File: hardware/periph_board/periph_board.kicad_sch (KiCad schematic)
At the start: 32 parts, among them IC100 CD74HC4067SM96, IC101 LM2937ET-3.3_NOPB, IC102 MCP3221AxT-E_OT, J100 2x8 Socket Pins, J101 2x8 Plug Pins

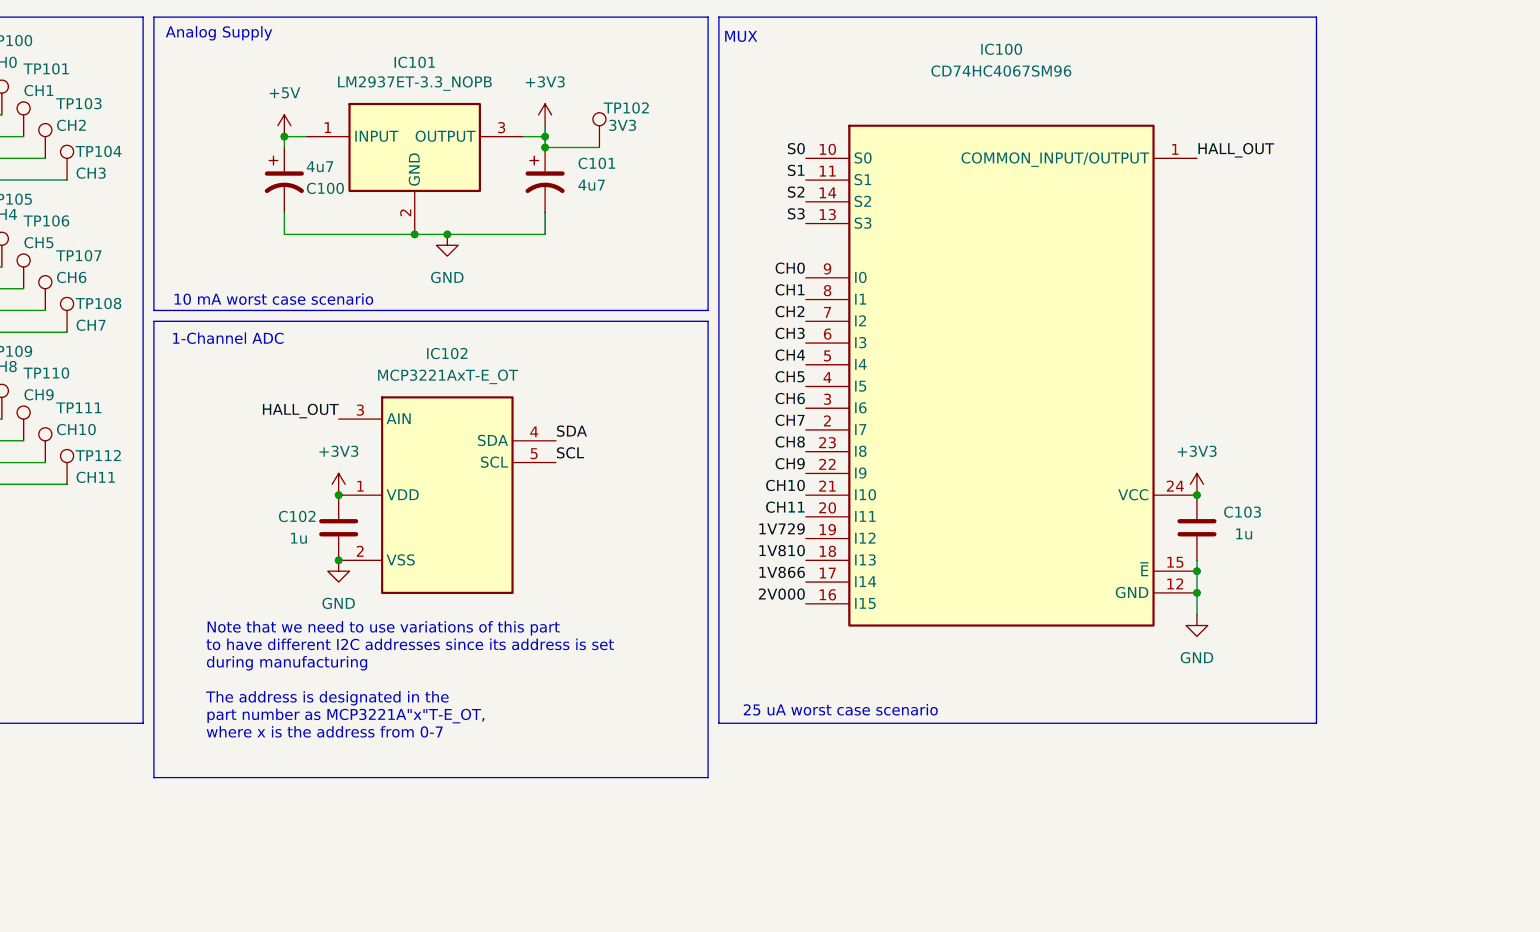
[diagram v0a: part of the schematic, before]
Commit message: added lakshay suggestions to peripheral board. removed bypass jumper from main board audio amp. added led strip interface. added too many things to remember i forgor
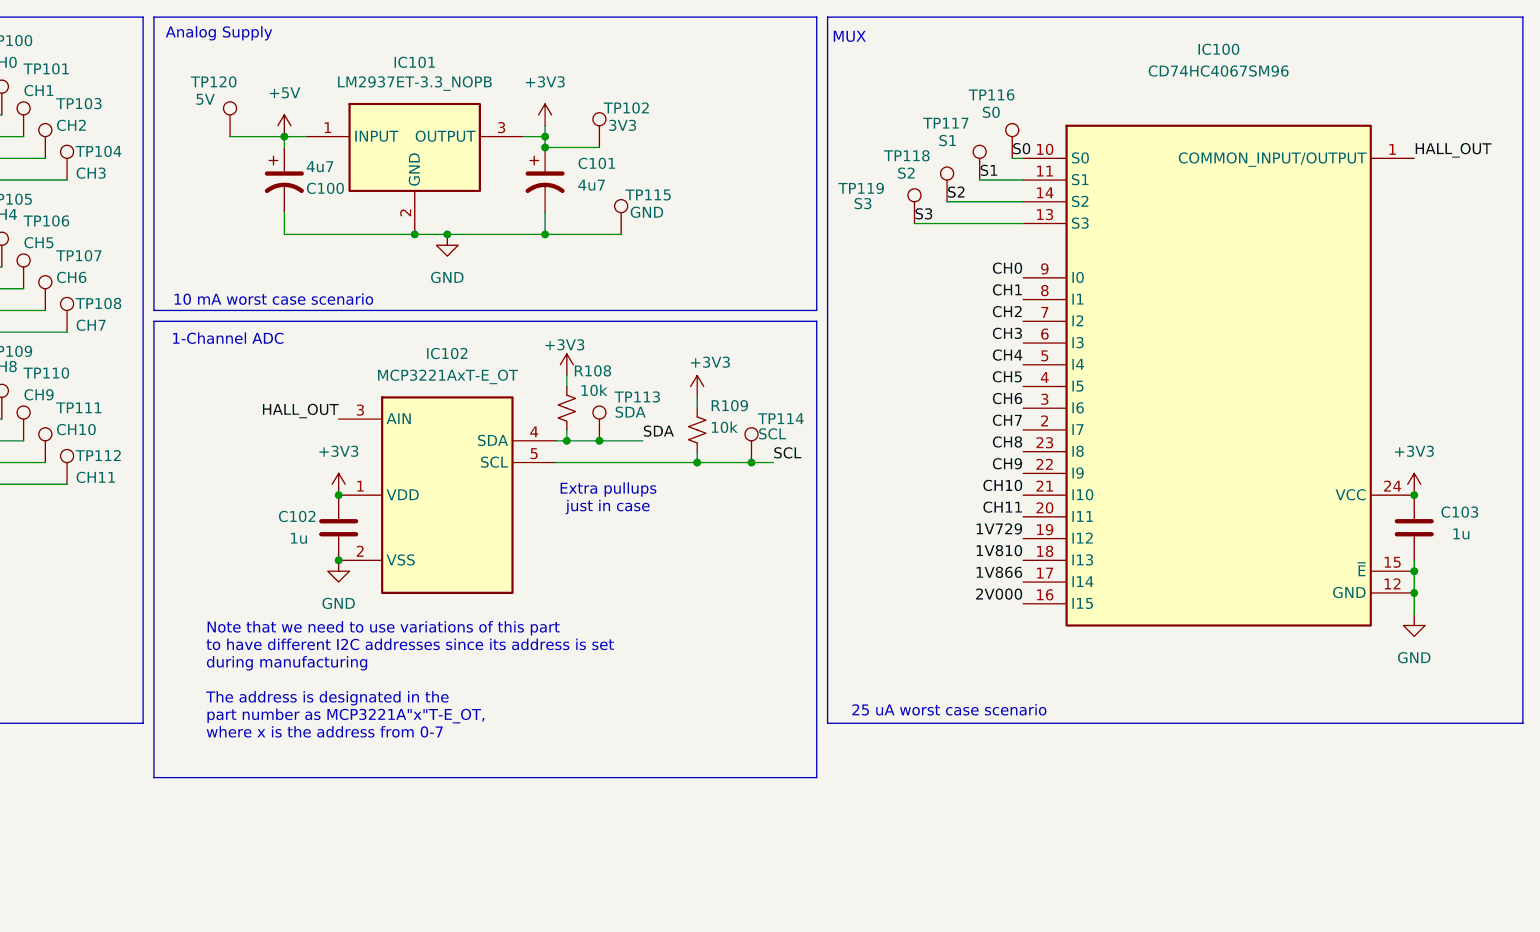
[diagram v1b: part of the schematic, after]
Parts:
- added R108, R109: 10k, Resistor_SMD:R_0805_2012Metric, symbol Device:R_Small_US
- added TP113: SDA, SamacSys_Parts:betterTestPoint_Pad_1.5x1.5mm, symbol Connector:TestPoint
- added TP114: SCL, SamacSys_Parts:betterTestPoint_Pad_1.5x1.5mm, symbol Connector:TestPoint
- added TP115: GND, SamacSys_Parts:bettertestpoint2, symbol Connector:TestPoint
- added TP116: S0, SamacSys_Parts:betterTestPoint_Pad_1.5x1.5mm, symbol Connector:TestPoint
- added TP117: S1, SamacSys_Parts:betterTestPoint_Pad_1.5x1.5mm, symbol Connector:TestPoint
- added TP118: S2, SamacSys_Parts:betterTestPoint_Pad_1.5x1.5mm, symbol Connector:TestPoint
- added TP119: S3, SamacSys_Parts:betterTestPoint_Pad_1.5x1.5mm, symbol Connector:TestPoint
- added TP120: 5V, SamacSys_Parts:bettertestpoint2, symbol Connector:TestPoint
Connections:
- net +3V3: now also R108.2, R109.2
- net +5V: now also TP120.1
- net GND: now also TP115.1
- net S0: now also TP116.1
- net S1: now also TP117.1
- net S2: now also TP118.1
- net S3: now also TP119.1
- net SCL: now also R109.1, TP114.1
- net SDA: now also R108.1, TP113.1
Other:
- note added: "Extra pullups just in case"
- moved on the sheet: C103, IC100
